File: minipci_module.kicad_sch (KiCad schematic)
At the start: 1 part, among them Con3 2041119-1

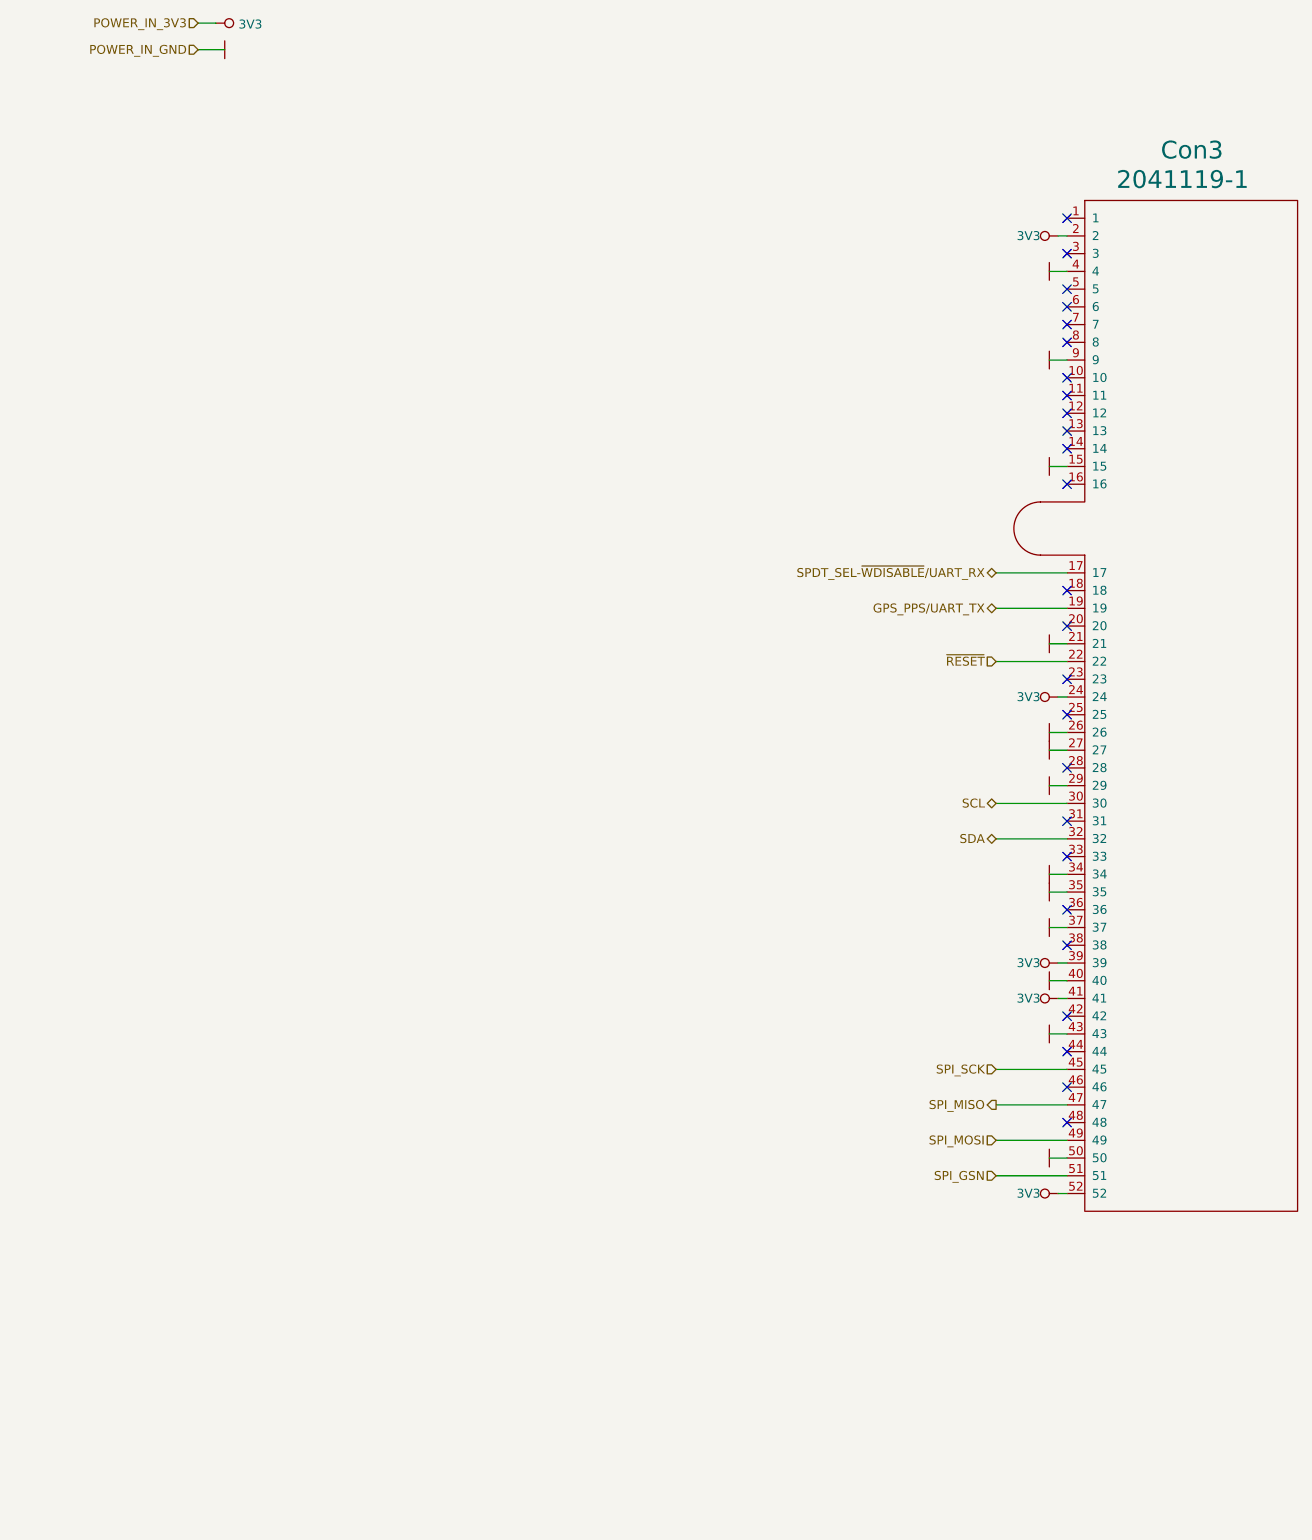
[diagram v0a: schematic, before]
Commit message: Corrected schematic
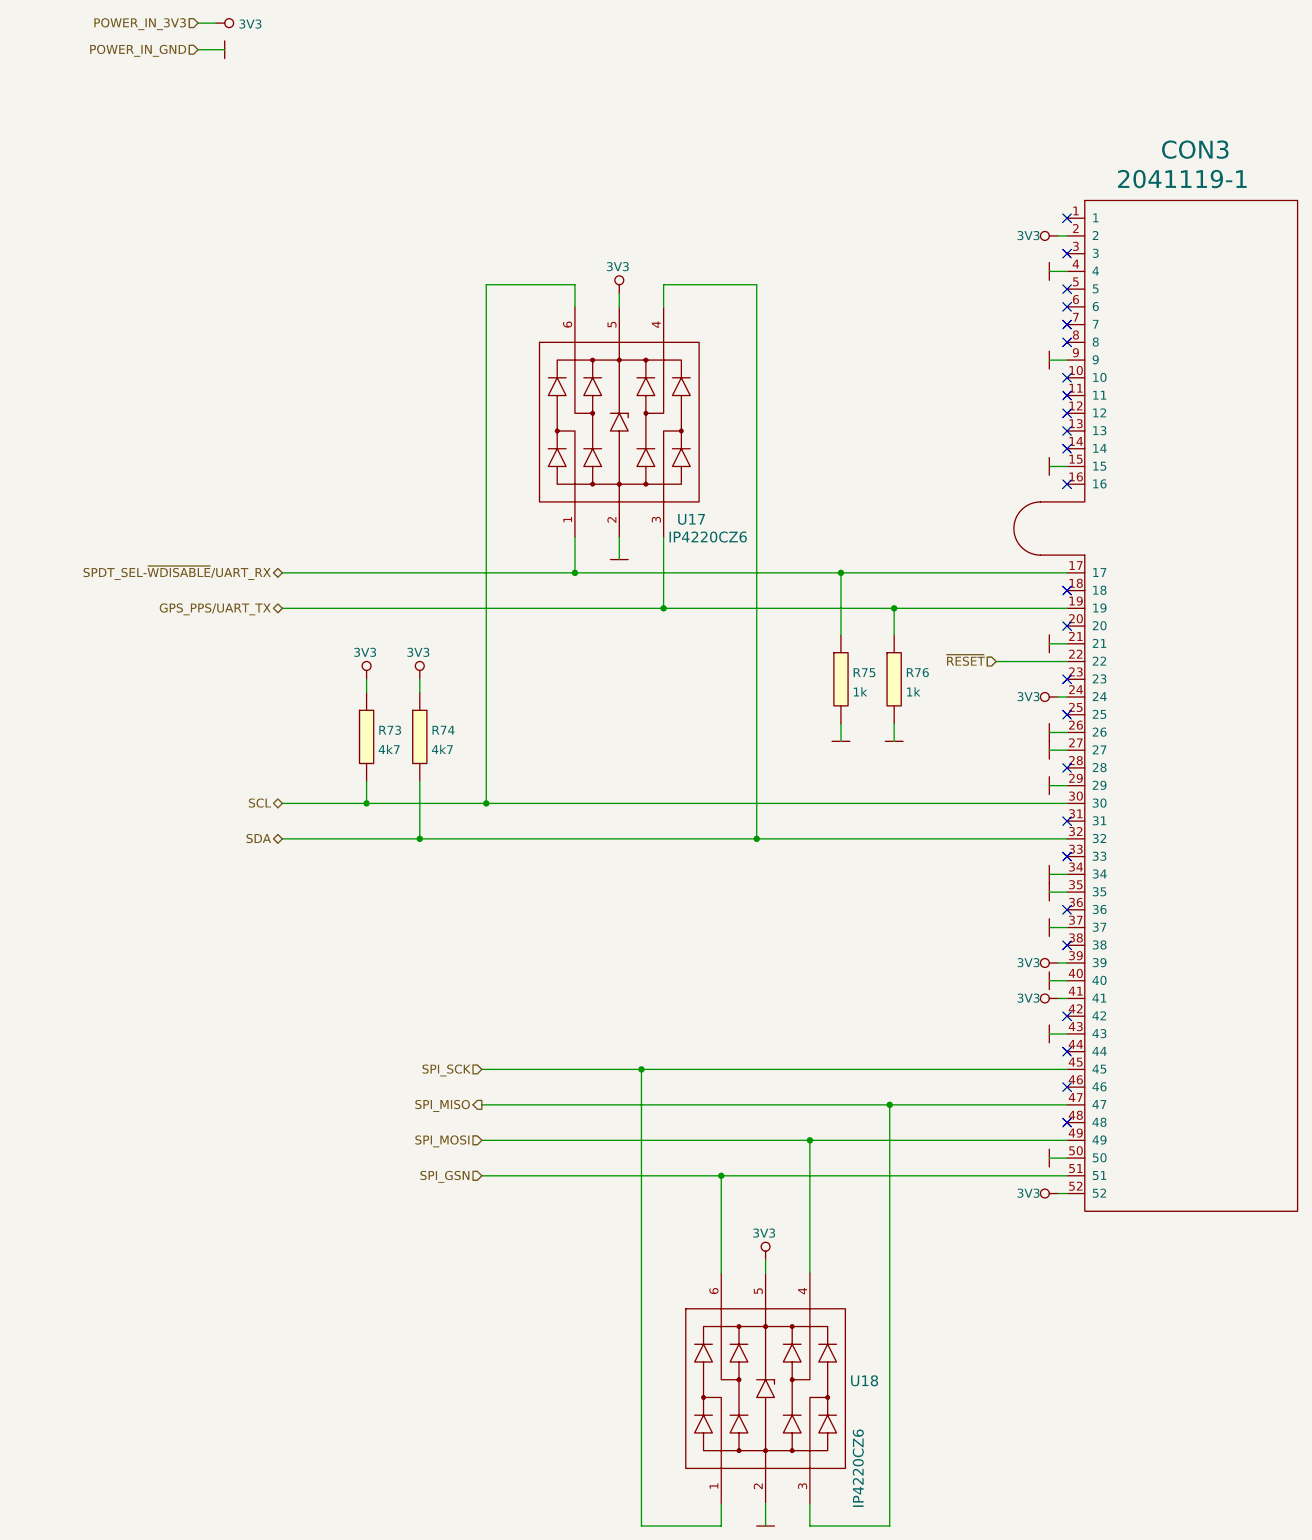
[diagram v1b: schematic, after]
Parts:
- added R73, R74: 4k7, Resistor_Smd_0402:4k7_0402, symbol Resistors_Smd0402:4k7
- added R75, R76: 1k, Resistor_Smd_0402:1k_0402, symbol Resistors_Smd0402:1k
- added U17, U18: IP4220CZ6, ESD_Protectors:IP4220CZ6_SOT457, symbol esd_protectors:IP4220CZ6
- renumbered Con3 to CON3
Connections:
- net 3V3: now also R73.1, R74.1, U17.5 (Vp), U18.5 (Vp)
- net GND: now also R75.2, R76.2, U17.2 (GND), U18.2 (GND)
- net GPS_PPS/UART_TX: now also R76.1, U17.3 (I/O2)
- net SCL: now also R73.2, U17.6 (I/O4)
- net SDA: now also R74.2, U17.4 (I/O3)
- net SPDT_SEL-~{WDISABLE}/UART_RX: now also R75.1, U17.1 (I/O1)
- net SPI_GSN: now also U18.6 (I/O4)
- net SPI_MISO: now also U18.3 (I/O2)
- net SPI_MOSI: now also U18.4 (I/O3)
- net SPI_SCK: now also U18.1 (I/O1)

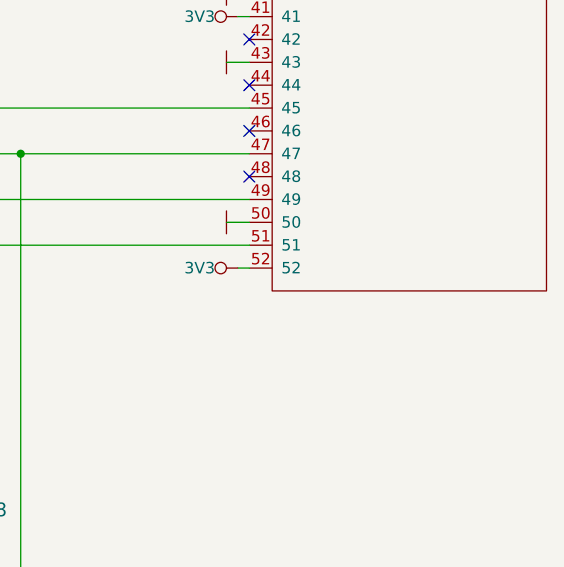
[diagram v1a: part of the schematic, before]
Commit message: Cleared all errors DRC
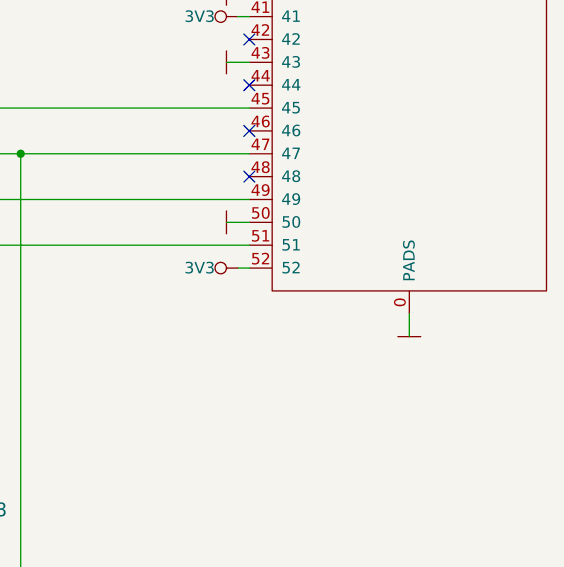
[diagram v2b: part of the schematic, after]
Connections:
- net GND: now also CON3.0 (PADS)
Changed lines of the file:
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@@
     (stroke (width 0) (type default) (color 0 0 0 0))
+  )
+  (wire (pts (xy 207.01 213.36) (xy 207.01 215.9))
+    (stroke (width 0) (type solid) (color 0 0 0 0))
   )
   (wire (pts (xy 96.52 134.62) (xy 96.52 136.525))
@@
       (effects (font (size 1.27 1.27)) hide)
     )
+    (pin "0")
     (pin "1")
     (pin "10")
@@
       (effects (font (size 1.524 1.524)))
     )
+    (pin "1")
+  )
+  (symbol (lib_id "power:GND") (at 207.01 215.9 0) (unit 1)
+    (in_bom yes) (on_board yes)
+    (property "Reference" "#PWR0232" (id 0) (at 207.01 213.36 0)
+      (effects (font (size 0.762 0.762)) hide)
+    )
+    (property "Value" "GND" (id 1) (at 207.01 218.44 0)
+      (effects (font (size 0.762 0.762)) hide)
+    )
+    (property "Footprint" "" (id 2) (at 207.01 215.9 0)
+      (effects (font (size 1.524 1.524)))
+    )
+    (property "Datasheet" "" (id 3) (at 207.01 215.9 0)
+      (effects (font (size 1.524 1.524)))
+    )

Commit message: Gerbers created, BOM, CPL
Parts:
- removed R73, R74: 4k7, Resistor_Smd_0402:4k7_0402, symbol Resistors_Smd0402:4k7
- removed R75, R76: 1k, Resistor_Smd_0402:1k_0402, symbol Resistors_Smd0402:1k
- added R73, R74: 4k7, Resistor_Smd_0603:4k7_0603, symbol Resistors_Smd0603:4k7
- added R75, R76: 1k, Resistor_Smd_0603:1k_0603, symbol Resistors_Smd0603:1k
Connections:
- net 3V3: now also R73.1, R74.1
- net GND: now also R75.2, R76.2
- net GPS_PPS/UART_TX: now also R76.1
- net SCL: now also R73.2
- net SDA: now also R74.2
- net SPDT_SEL-~{WDISABLE}/UART_RX: now also R75.1

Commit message: New branch created
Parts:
- removed CON3: 2041119-1, Smd_Connectors:2041119-1, symbol Smd_Connectors:2041119-1
- added CON3: (no value), symbol Smd_Connectors:119A-80A00-R02-SET
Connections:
- net 3V3: now also CON3.2, CON3.24, CON3.39, CON3.41, CON3.52
- net GND: now also CON3.0 (PADS), CON3.15, CON3.21, CON3.26, CON3.27, CON3.29, CON3.34, CON3.35, CON3.37, CON3.4, CON3.40, CON3.43, CON3.50, CON3.9
- net GPS_PPS/UART_TX: now also CON3.19
- net SCL: now also CON3.30
- net SDA: now also CON3.32
- net SPDT_SEL-~{WDISABLE}/UART_RX: now also CON3.17
- net SPI_GSN: now also CON3.51
- net SPI_MISO: now also CON3.47
- net SPI_MOSI: now also CON3.49
- net SPI_SCK: now also CON3.45
- net ~{RESET}: now also CON3.22

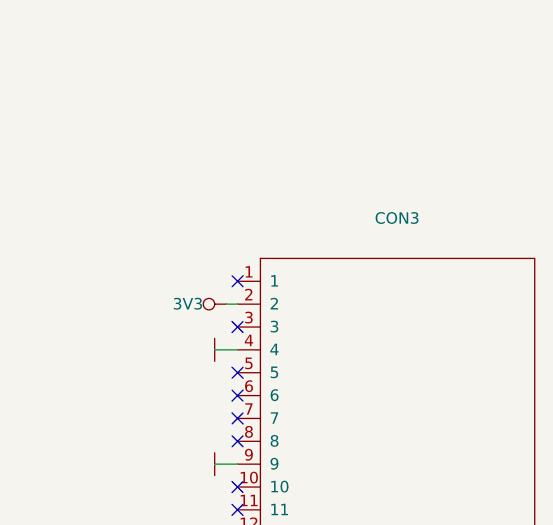
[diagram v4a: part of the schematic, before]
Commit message: Changed ethernet connector to horizontal and changed it position to avoid collision with arduino shield
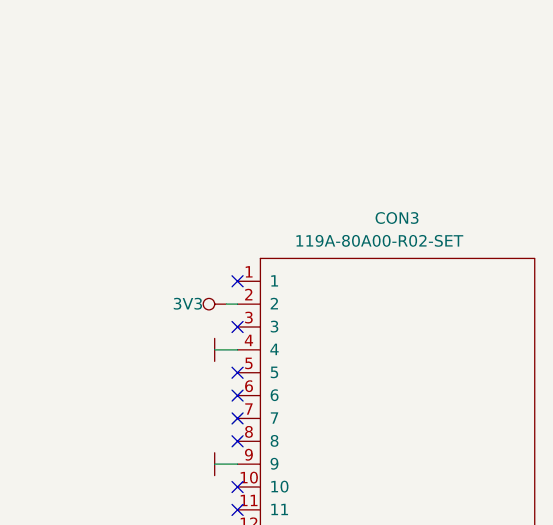
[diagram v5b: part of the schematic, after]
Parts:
- CON3: value (none) -> 119A-80A00-R02-SET; footprint (none) -> Smd_Connectors:119A-80A00-R02-SET
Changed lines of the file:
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@@
       (effects (font (size 1.27 1.27)) (justify left))
     )
-    (property "Value" "" (id 1) (at 195.58 64.135 0)
+    (property "Value" "119A-80A00-R02-SET" (id 1) (at 195.58 64.135 0)
       (effects (font (size 1.27 1.27)) (justify left))
     )
-    (property "Footprint" "" (id 2) (at 279.4 148.59 0)
+    (property "Footprint" "Smd_Connectors:119A-80A00-R02-SET" (id 2) (at 279.4 148.59 0)
       (effects (font (size 2.54 2.54)) hide)
     )
